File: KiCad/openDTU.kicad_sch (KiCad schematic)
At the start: 46 parts, among them J1 USB_C_Receptacle_USB2.0, J2 Conn_Coaxial, J3 Micro_SD_Card, J4 Conn_02x05_Counter_Clockwise, Q1 BC817, Q2 BC817, SW1 SW_Push, SW2 SW_Push, U1 CH340C, U3 ESP32-WROOM-32, U4 nRF24L01P, U5 NCP1117-3.3_SOT223, Y1 Crystal

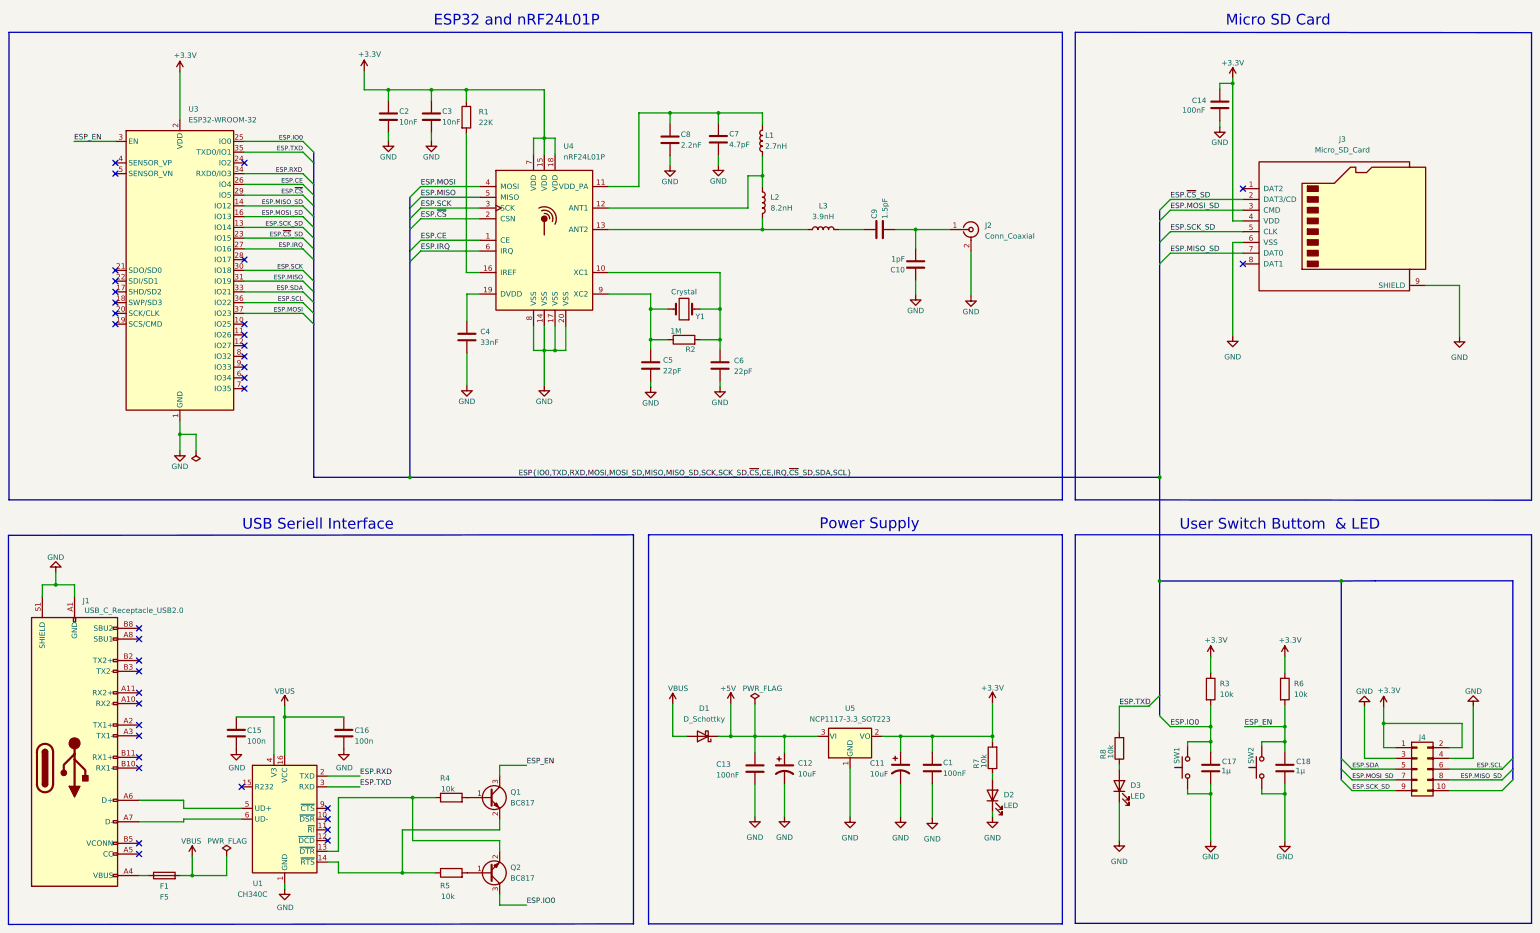
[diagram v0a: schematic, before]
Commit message: all tracks first time routed
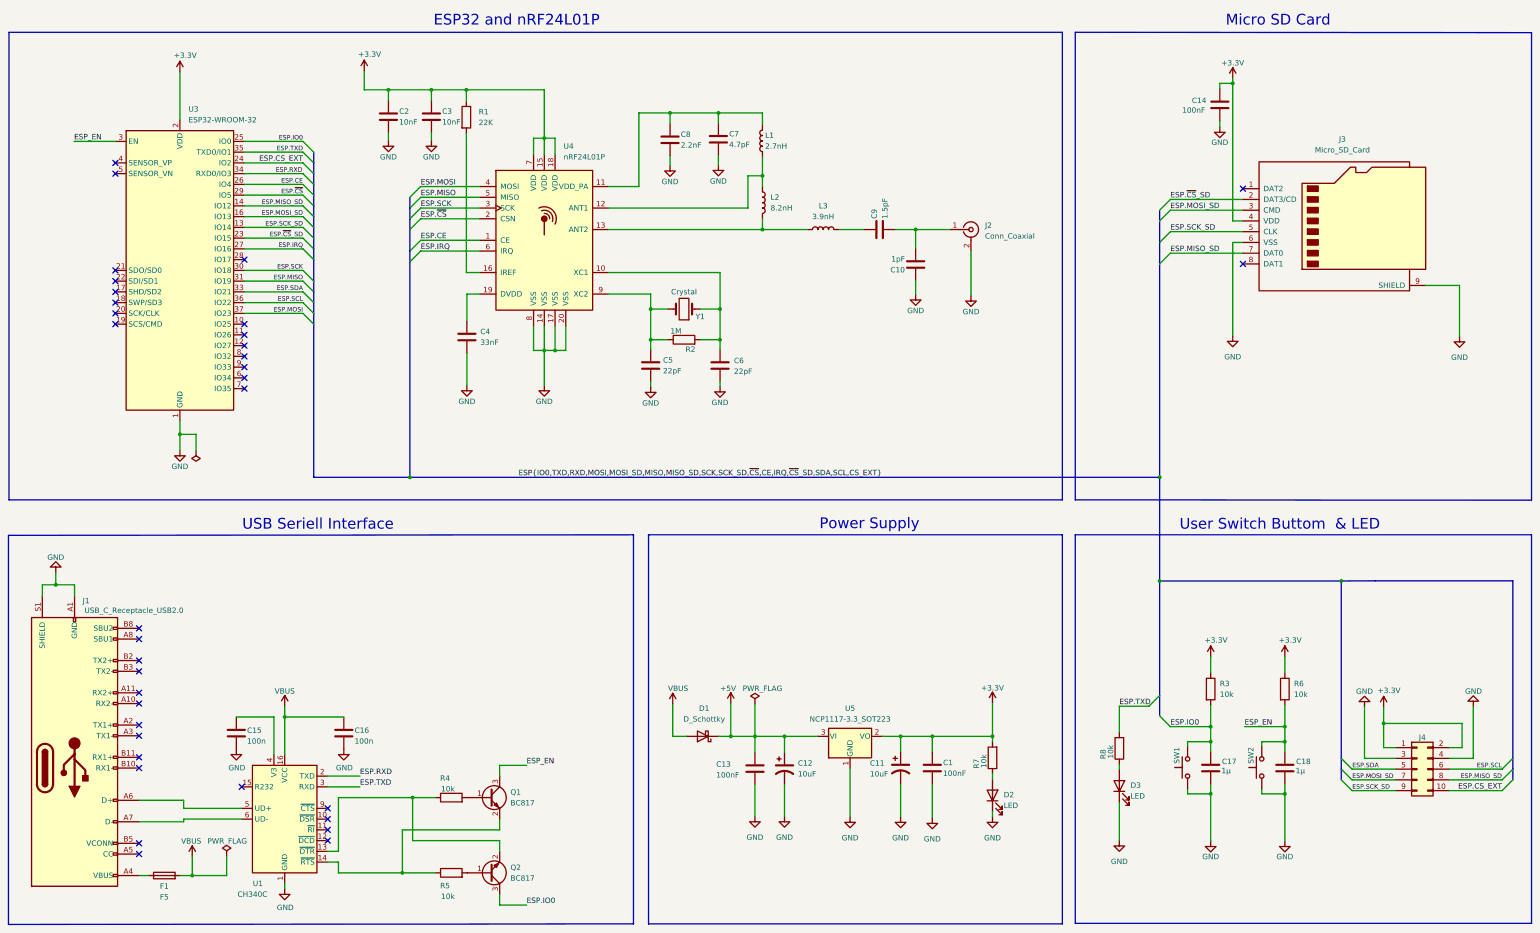
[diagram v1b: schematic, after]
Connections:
- net ESP.CS_EXT: now reaches J4.10 (Pin_10)
- net ESP.CS_EXT: now also U3.24 (IO2)
- no-connect marks 36 -> 35

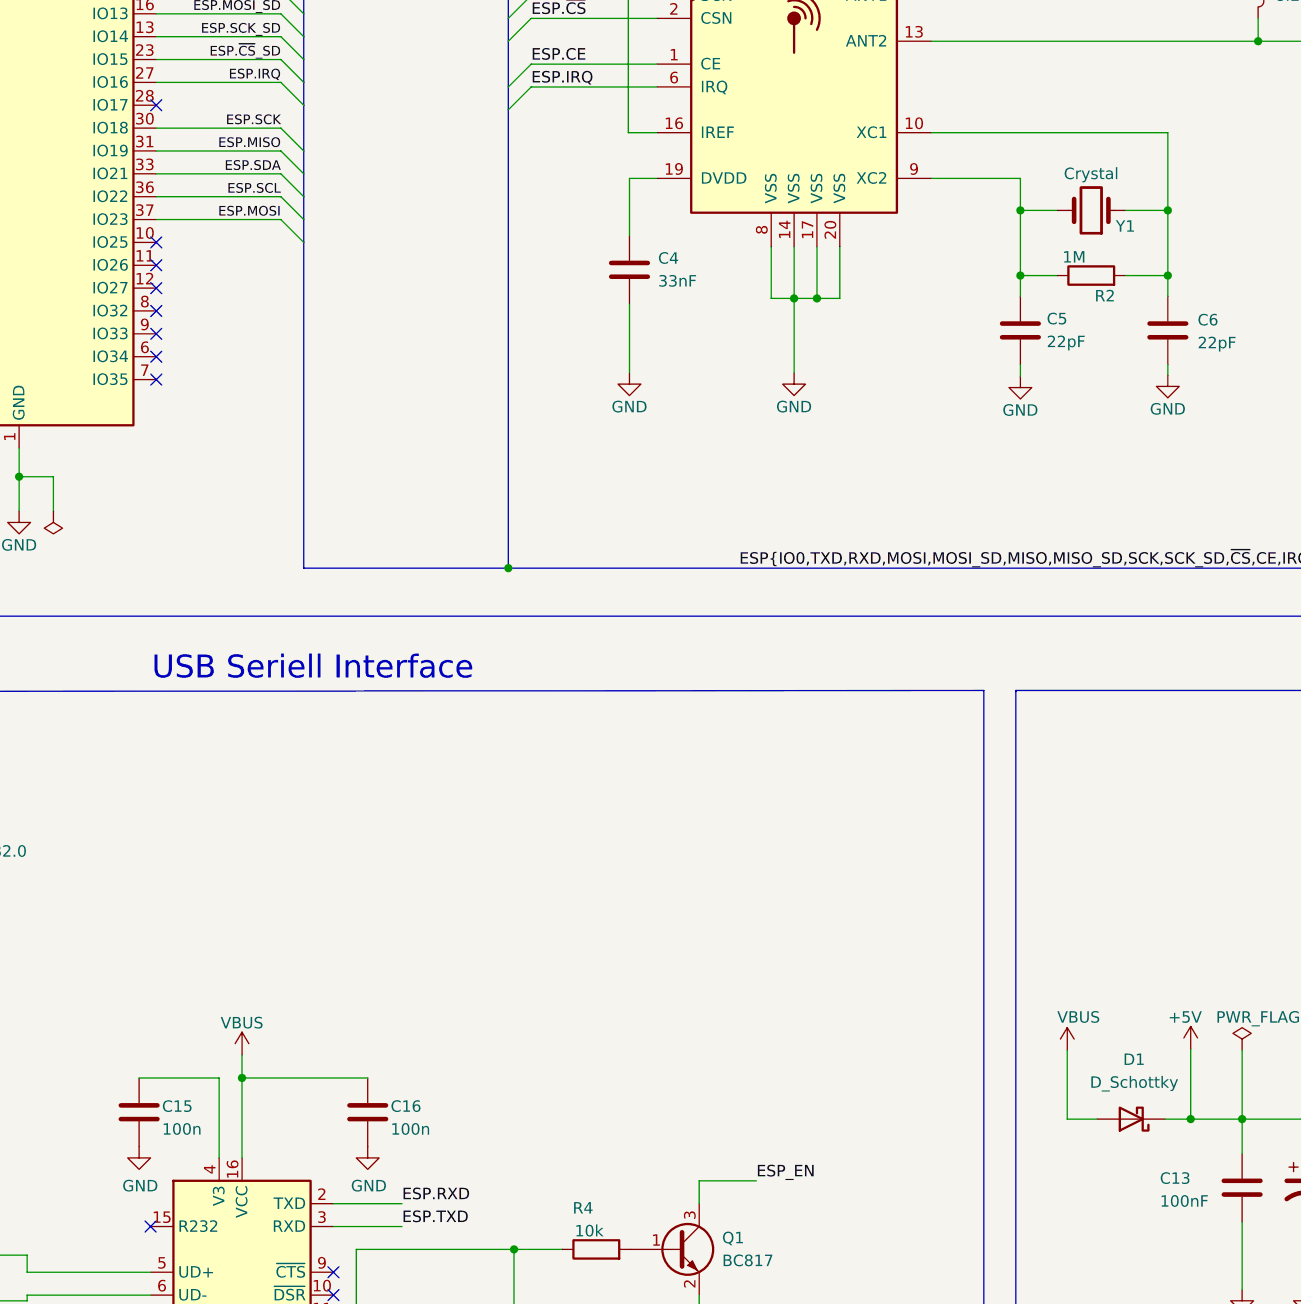
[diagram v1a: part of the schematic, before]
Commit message: adding Frequency value to crystal an fixing crystal pin/footrpint assignment
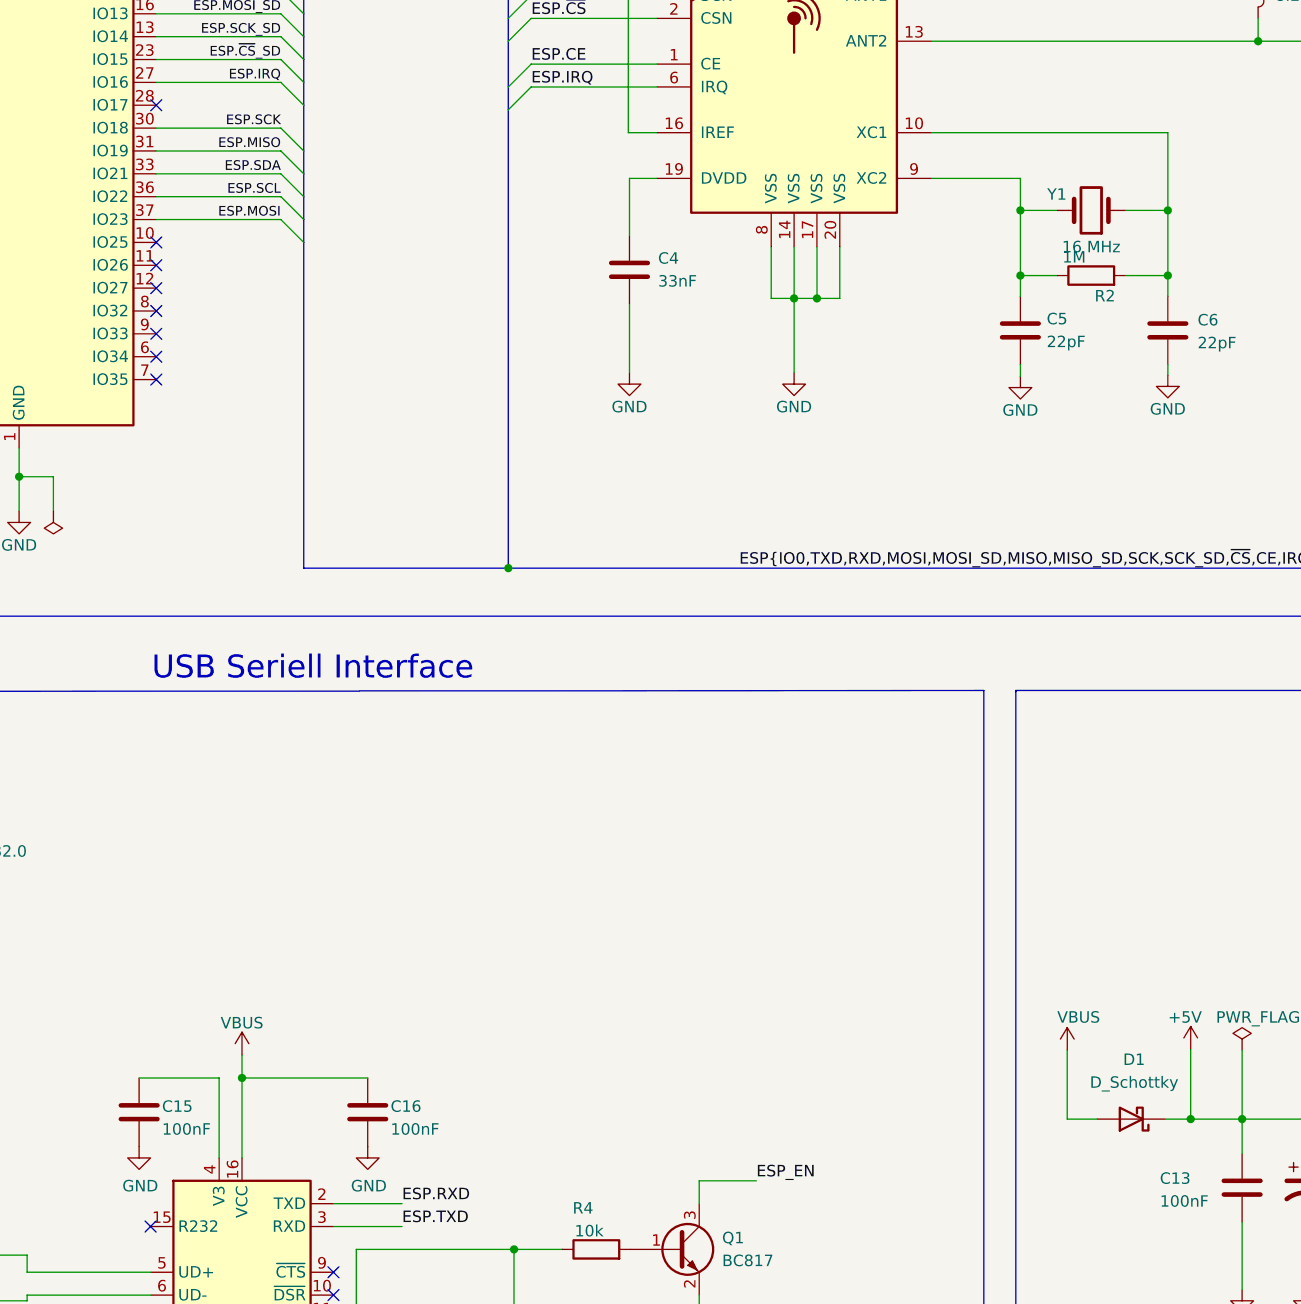
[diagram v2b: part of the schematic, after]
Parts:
- C15, C16: value 100n -> 100nF
- Y1: value Crystal -> 16 MHz
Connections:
- net at C5.1, R2.1, U4.9 (XC2): now also Y1.3; no longer Y1.2
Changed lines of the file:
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@@
   (symbol (lib_id "Device:Crystal") (at 193.421 91.694 180) (unit 1)
     (in_bom yes) (on_board yes)
-    (property "Reference" "Y1" (id 0) (at 197.231 93.472 0))
-    (property "Value" "Crystal" (id 1) (at 193.421 87.63 0))
+    (property "Reference" "Y1" (id 0) (at 189.611 89.916 0))
+    (property "Value" "16 MHz" (id 1) (at 193.421 95.758 0))
     (property "Footprint" "Crystal:Crystal_SMD_3225-4Pin_3.2x2.5mm" (id 2) (at 193.421 91.694 0)
       (effects (font (size 1.27 1.27)) hide)
@@
     )
     (pin "1")
-    (pin "2")
+    (pin "3")
   )
   (symbol (lib_id "Device:LED") (at 266.319 206.629 90) (unit 1)
@@
       (effects (font (size 1.27 1.27)) (justify left))
     )
-    (property "Value" "100n" (id 1) (at 115.57 193.802 0)
+    (property "Value" "100nF" (id 1) (at 115.57 193.802 0)
       (effects (font (size 1.27 1.27)) (justify left))
     )
@@
       (effects (font (size 1.27 1.27)) (justify left))
     )
-    (property "Value" "100n" (id 1) (at 90.17 193.802 0)
+    (property "Value" "100nF" (id 1) (at 90.17 193.802 0)
       (effects (font (size 1.27 1.27)) (justify left))
     )
@@
     )
     (path "/dc506d58-594e-475d-ad98-724550a69c5e"
-      (reference "C15") (unit 1) (value "100n") (footprint "Capacitor_SMD:C_0603_1608Metric")
+      (reference "C15") (unit 1) (value "100nF") (footprint "Capacitor_SMD:C_0603_1608Metric")
     )
     (path "/d2985c6a-d249-43df-a8ee-7a1064bccba6"
-      (reference "C16") (unit 1) (value "100n") (footprint "Capacitor_SMD:C_0603_1608Metric")
+      (reference "C16") (unit 1) (value "100nF") (footprint "Capacitor_SMD:C_0603_1608Metric")
     )
     (path "/f9e8beb9-10a0-4bf9-897a-4fd73218fd25"
@@
     )
     (path "/1e16fe82-9c55-4ee7-9530-e7058aa0265c"
-      (reference "Y1") (unit 1) (value "Crystal") (footprint "Crystal:Crystal_SMD_3225-4Pin_3.2x2.5mm")
-    )
-  )
+      (reference "Y1") (unit 1) (value "16 MHz") (footprint "Crystal:Crystal_SMD_3225-4Pin_3.2x2.5mm")
+    )
+  )
